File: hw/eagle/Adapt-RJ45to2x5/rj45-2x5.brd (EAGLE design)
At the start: 32.3 x 44 mm, 5 parts, among them P11 SOLPAD035, P21 SOLPAD035

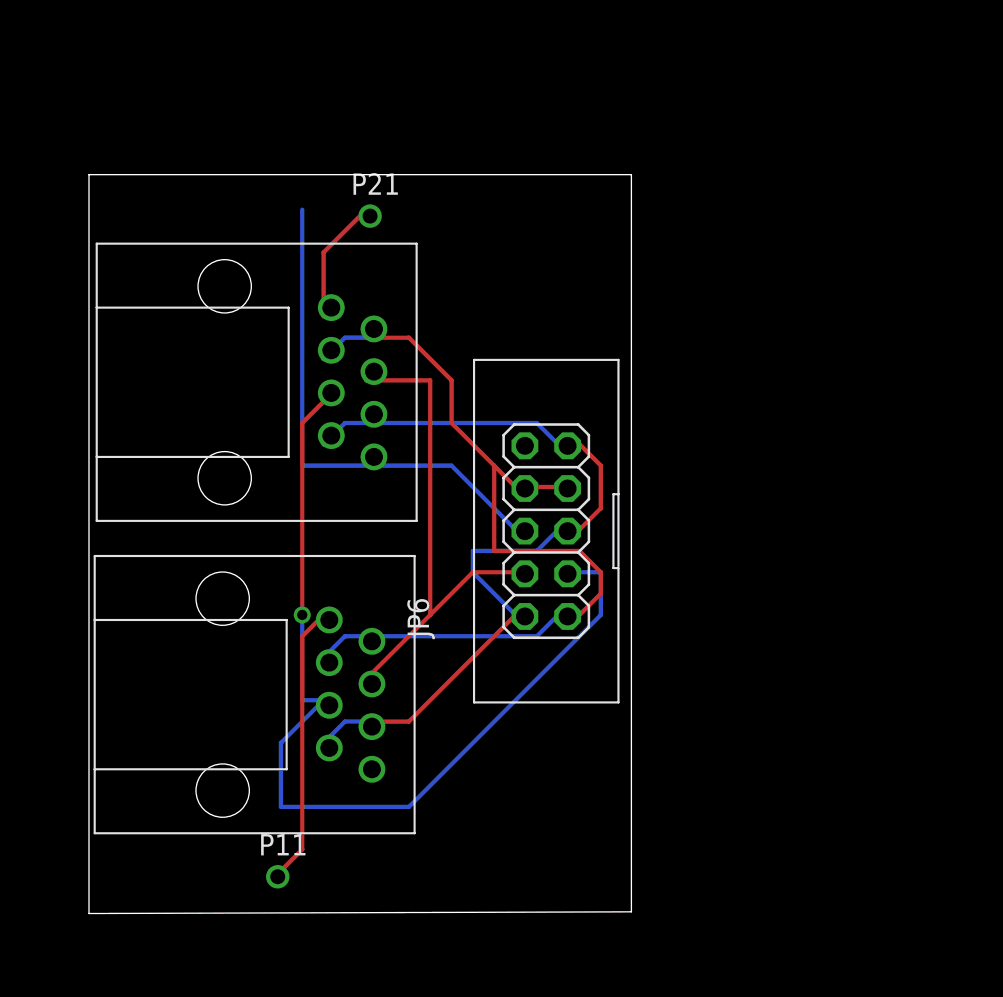
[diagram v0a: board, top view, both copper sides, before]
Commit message: add rj45-2x10 adaptor eagle files
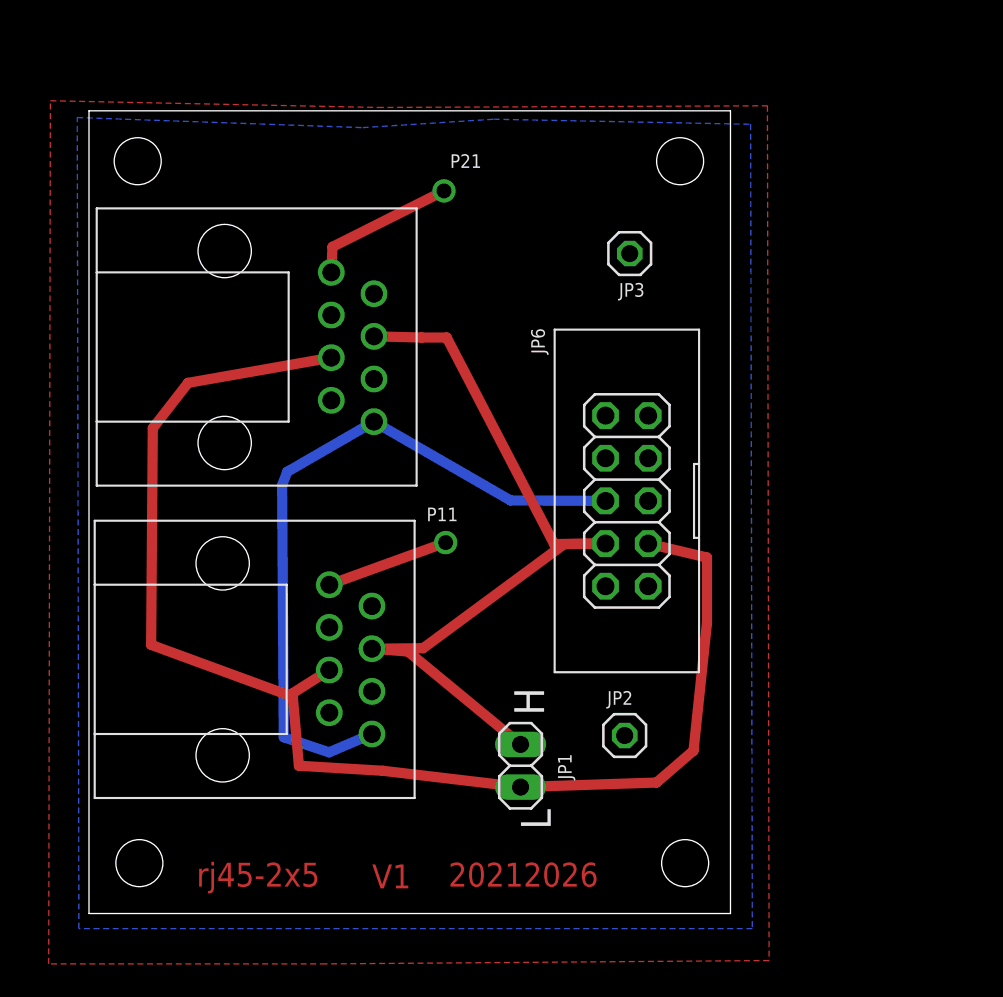
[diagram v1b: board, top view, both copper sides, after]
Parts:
- added JP1: CAN, pinhead:1X02
- added JP2: +12V, pinhead:1X01
- added JP3: GND, pinhead:1X01
- JP6: value PINHD-2X5_KEYED -> BMS ribbon
- moved P11 22.3 mm to (21.2, 22.1)
- moved JP6 5.13 mm to (32.0, 24.6)
- moved P21 4.65 mm to (21.1, 43.0)
- moved JP8 2.10 mm to (16.9, 15.8)
- moved JP7 2.10 mm to (17.0, 34.4)
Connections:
- net +12V: now also JP2.1
- net CANH: now also JP1.1
- net CANL: now also JP1.2
- net GNDA: now also JP3.1
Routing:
- net +12V: track 54.6 -> 0.00 mm
- net GNDA: track 52.7 -> 0.00 mm
- net CANL: track 56.4 -> 80.3 mm, vias 1 -> 0
- net CANH: track 31.0 -> 48.1 mm
- net MASTER-RESET-SYS: track 30.8 -> 42.5 mm
- net CANCABLE_1_1: track 17.1 -> 7.37 mm
- added copper zone on layer 1, net +12V
- added copper zone on layer 16, net GNDA
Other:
- board size 32.3 x 44 mm -> 38.2 x 47.8 mm
- board text added: "20212026"
- board text added: "H"
- board text added: "L"
- board text added: "V1"
- board text added: "rj45-2x5"

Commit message: update of pcbs. save work
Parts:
- added JP4: BMS ribbon, pinhead:2X05_KEYED
- added JP5: M-RESET, pinhead:1X01
- moved JP2 20.4 mm to (12.8, 3.40)
- moved JP3 20.1 mm to (12.9, 44.9)
- moved JP6 13.3 mm to (36.3, 12.0)
- moved JP1 2.91 mm to (25.5, 5.90)
- moved P21 1.77 mm to (20.6, 44.7)
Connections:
- new net N$2: JP4.10, JP6.10
- net +12V: now also JP4.1, JP4.7, JP4.8
- net CANH: now also JP4.4
- net CANL: now also JP4.3
- net GNDA: now also JP4.2, JP4.5, JP4.9
- net MASTER-RESET-SYS: now also JP4.6, JP5.1
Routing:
- net N$2: track 0.00 -> 37.6 mm, vias 0 -> 1
- net MASTER-RESET-SYS: track 42.5 -> 65.9 mm
- net CANL: track 80.3 -> 100.5 mm
- net CANH: track 48.1 -> 66.6 mm
- net +12V: track 0.00 -> 11.6 mm
- net CANCABLE_2_1: track 8.95 -> 9.46 mm
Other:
- board size 38.2 x 47.8 mm -> 49.7 x 49.8 mm
- board text added: "+12V"
- board text added: "20220103"
- board text added: "Adapt-RJ45to2x5/rj45-2x5"
- board text added: "CAN"
- board text added: "GND"
- board text added: "MASTER"
- board text added: "PIN 1"
- board text added: "RESET"
- board text removed: "20212026"

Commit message: 14921 pcb updates. DUMP 3 pin, plus VOred pin added
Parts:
- added JP9: 12V, pinhead:1X02
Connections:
- net +12V: now also JP9.2
- net GNDA: now also JP9.1
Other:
- board text added: "+12"
- board text added: "+12v"
- board text added: "1"
- board text added: "12V POWER"
- board text added: "8"
- board text added: "G"
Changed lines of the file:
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@@
 <text x="22.6" y="12.9" size="1.016" layer="25">MASTER</text>
 <text x="23.5" y="11.4" size="1.016" layer="25">RESET</text>
-<text x="23.5" y="20.5" size="1.016" layer="25" rot="R90">PIN 1</text>
-<text x="22.9" y="43.2" size="1.016" layer="25" rot="R90">PIN 1</text>
+<text x="23.1" y="24.4" size="1.016" layer="25" rot="R180">PIN 1</text>
+<text x="21.1" y="46.9" size="1.016" layer="25" rot="R180">PIN 1</text>
 <text x="15.6" y="43.4" size="1.016" layer="25" rot="R90">GND</text>
 <text x="15.3" y="1.9" size="1.016" layer="25" rot="R90">+12V</text>
@@
 <hole x="46.8" y="46.8" drill="3.2"/>
 <hole x="46.8" y="3.2" drill="3.2"/>
+<text x="21.9" y="42.1" size="1.016" layer="25">12V POWER</text>
+<text x="22.5" y="47.6" size="0.8128" layer="25">GND</text>
+<text x="27.4" y="47.6" size="0.8128" layer="25">+12</text>
+<text x="13.5" y="39" size="0.8128" layer="26" rot="MR0">1</text>
+<text x="13.5" y="21" size="0.8128" layer="26" rot="MR0">1</text>
+<text x="18.3" y="9" size="0.8128" layer="26" rot="MR0">8</text>
+<text x="18.4" y="27.7" size="0.8128" layer="26" rot="MR0">8</text>
+<text x="25.7" y="42.7" size="0.8128" layer="26" rot="MR0">+12v</text>
+<text x="20.5" y="46.1" size="0.8128" layer="26" rot="MR0">+12v</text>
+<text x="13.6" y="5.2" size="0.8128" layer="26" rot="MR0">+12v</text>
+<text x="19.9" y="38.1" size="0.8128" layer="26" rot="MR0">+12v</text>
+<text x="19.7" y="19.5" size="0.8128" layer="26" rot="MR0">+12v</text>
+<text x="33.5" y="14.5" size="0.8128" layer="26" rot="MR0">+12</text>
+<text x="41.2" y="14.3" size="0.8128" layer="26" rot="MR0">+12</text>
+<text x="41.1" y="6.5" size="0.8128" layer="26" rot="MR0">+12</text>
+<text x="40.9" y="30" size="0.8128" layer="26" rot="MR0">+12</text>
+<text x="41.1" y="37.6" size="0.8128" layer="26" rot="MR0">+12</text>
+<text x="33.5" y="37.6" size="0.8128" layer="26" rot="MR0">+12</text>
+<text x="40.1" y="40.2" size="0.8128" layer="26" rot="MR0">G</text>
+<text x="40.3" y="34.9" size="0.8128" layer="26" rot="MR0">G</text>
+<text x="33.3" y="29.8" size="0.8128" layer="26" rot="MR0">G</text>
+<text x="40.1" y="16.8" size="0.8128" layer="26" rot="MR0">G</text>
+<text x="40.1" y="11.7" size="0.8128" layer="26" rot="MR0">G</text>
+<text x="33.3" y="6.7" size="0.8128" layer="26" rot="MR0">G</text>
+<text x="19.5" y="12.6" size="0.8128" layer="26" rot="MR0">G</text>
+<text x="19.4" y="31.5" size="0.8128" layer="26" rot="MR0">G</text>
+<text x="28.3" y="42.6" size="0.8128" layer="26" rot="MR0">G</text>
+<text x="13.3" y="46.5" size="0.8128" layer="26" rot="MR0">G</text>
+<text x="13" y="29.8" size="0.8128" layer="26" rot="MR0">G</text>
+<text x="12.9" y="11.2" size="0.8128" layer="26" rot="MR0">G</text>
+<text x="13.1" y="35.7" size="0.8128" layer="26" rot="MR0">+12v</text>
+<text x="12.9" y="16.6" size="0.8128" layer="26" rot="MR0">+12v</text>
+<text x="23.2" y="6.9" size="0.8128" layer="26" rot="MR0">H</text>
+<text x="22.8" y="4.4" size="0.8128" layer="26" rot="MR0">L</text>
+<text x="33.5" y="32.5" size="0.8128" layer="26" rot="MR0">H</text>
+<text x="33.5" y="9.1" size="0.8128" layer="26" rot="MR0">H</text>
+<text x="19.3" y="34.2" size="0.8128" layer="26" rot="MR0">H</text>
+<text x="19.2" y="15.4" size="0.8128" layer="26" rot="MR0">H</text>
+<text x="12.5" y="14.2" size="0.8128" layer="26" rot="MR0">L</text>
+<text x="12.6" y="32.8" size="0.8128" layer="26" rot="MR0">L</text>
+<text x="39.8" y="32.3" size="0.8128" layer="26" rot="MR0">L</text>
+<text x="39.8" y="9.2" size="0.8128" layer="26" rot="MR0">L</text>
 </plain>
 <attributes>
@@
 <element name="JP8" library="DEH" package="MOD8P8C" value="" x="16.85" y="15.77" rot="R270"/>
 <element name="P11" library="solpad" package="SOLDPAD035" value="SOLPAD035" x="21.24" y="22.09" locked="yes" smashed="yes">
-<attribute name="NAME" x="20.097" y="23.36" size="0.8128" layer="25" ratio="10"/>
+<attribute name="NAME" x="19.697" y="20.26" size="0.8128" layer="25" ratio="10"/>
 </element>
 <element name="P21" library="solpad" package="SOLDPAD035" value="SOLPAD035" x="20.64" y="44.73" smashed="yes">
-<attribute name="NAME" x="18.397" y="45.7" size="0.8128" layer="25" ratio="10"/>
+<attribute name="NAME" x="17.897" y="43" size="0.8128" layer="25" ratio="10"/>
 </element>
 <element name="JP1" library="pinhead" package="1X02" value="CAN" x="25.5" y="5.9" smashed="yes" rot="R270">
@@
 <attribute name="NAME" x="23.9538" y="17.3288" size="0.8128" layer="25" ratio="10"/>
 <attribute name="VALUE" x="24.03" y="12.325" size="1.27" layer="27"/>
+</element>
+<element name="JP9" library="pinhead" package="1X02" value="12V" x="26.2" y="45.6" smashed="yes" rot="R180">
+<attribute name="NAME" x="22.6288" y="46.4162" size="0.8128" layer="25" ratio="10" rot="R270"/>
+<attribute name="VALUE" x="28.74" y="48.775" size="1.27" layer="27" rot="R180"/>
 </element>
 </elements>
@@
 <contactref element="JP4" pad="5"/>
 <contactref element="JP4" pad="9"/>
+<contactref element="JP9" pad="1"/>
 </signal>
 <signal name="+12V">
@@
 <wire x1="37.6" y1="6.89" x2="42.3" y2="7.7" width="0.6096" layer="1"/>
 <wire x1="42.3" y1="7.7" x2="42.6" y2="14.5" width="0.6096" layer="1"/>
+<contactref element="JP9" pad="2"/>
 </signal>
 <signal name="CANL">
